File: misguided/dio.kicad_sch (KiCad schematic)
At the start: 0 parts

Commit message: buncha stuff
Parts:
- added CR401, CR402: LTV-217-TP1-C-G, LTV_217_LTO, symbol misguided:LTV-217-TP1-C-G
- added R401: 1k, symbol Device:R
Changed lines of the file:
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@@
 (kicad_sch (version 20230121) (generator eeschema)
   (paper "A4")
+  (hierarchical_label "DOUT_REF" (shape input) (at 131.445 92.71 0) (fields_autoplaced)
+    (effects (font (size 1.27 1.27)) (justify left))
+  )
+  (hierarchical_label "DOUT" (shape output) (at 121.92 95.25 0) (fields_autoplaced)
+    (effects (font (size 1.27 1.27)) (justify left))
+  )
+  (hierarchical_label "OUTPUT_GPIO" (shape input) (at 96.52 95.25 180) (fields_autoplaced)
+    (effects (font (size 1.27 1.27)) (justify right))
+  )
+  (hierarchical_label "DOUT_GND" (shape input) (at 132.08 100.33 0) (fields_autoplaced)
+    (effects (font (size 1.27 1.27)) (justify left))
+  )
+  (hierarchical_label "DIN" (shape input) (at 121.92 64.135 0) (fields_autoplaced)
+    (effects (font (size 1.27 1.27)) (justify left))
+  )
+  (hierarchical_label "DIN_GND" (shape input) (at 121.92 66.04 0) (fields_autoplaced)
+    (effects (font (size 1.27 1.27)) (justify left))
+  )
+  (hierarchical_label "INPUT_GPIO" (shape output) (at 96.52 64.135 180) (fields_autoplaced)
+    (effects (font (size 1.27 1.27)) (justify right))
+  )
+  (symbol (lib_id "Device:R") (at 119.38 90.17 0) (unit 1)
+    (in_bom yes) (on_board yes) (dnp no) (fields_autoplaced)
+    (property "Reference" "R401" (at 121.92 89.535 0)
+      (effects (font (size 1.27 1.27)) (justify left))
+    )
+    (property "Value" "1k" (at 121.92 92.075 0)
+      (effects (font (size 1.27 1.27)) (justify left))
+    )
+    (property "Footprint" "" (at 117.602 90.17 90)
+      (effects (font (size 1.27 1.27)) hide)
+    )
+    (property "Datasheet" "~" (at 119.38 90.17 0)
+      (effects (font (size 1.27 1.27)) hide)
+    )
+    (pin "1")
+    (pin "2")
+    (instances
+      (project "misguided"
+        (path "/2c6152e0-1c3c-4f15-8d1e-fd42bd51bc79/6cc4a32d-403e-4907-919c-d415739d9e80"
+          (reference "R401") (unit 1)
+        )
+      )
+    )
+  )
+  (symbol (lib_id "misguided:LTV-217-TP1-C-G") (at 103.505 111.76 0) (unit 1)
+    (in_bom yes) (on_board yes) (dnp no) (fields_autoplaced)
+    (property "Reference" "CR402" (at 103.505 104.14 0)
+      (effects (font (size 1.524 1.524)))
+    )
+    (property "Value" "LTV-217-TP1-C-G" (at 103.505 106.68 0)
+      (effects (font (size 1.524 1.524)))
+    )
+    (property "Footprint" "LTV_217_LTO" (at 103.505 119.38 0)
+      (effects (font (size 1.27 1.27) italic) hide)
+    )
+    (property "Datasheet" "LTV-217-TP1-C-G" (at 103.505 121.92 0)
+      (effects (font (size 1.27 1.27) italic) hide)
+    )
+    (pin "1")
+    (pin "2")
+    (pin "3")
+    (pin "4")
+    (instances
+      (project "misguided"
+        (path "/2c6152e0-1c3c-4f15-8d1e-fd42bd51bc79/6cc4a32d-403e-4907-919c-d415739d9e80"
+          (reference "CR402") (unit 1)
+        )
+      )
+    )
+  )
+  (symbol (lib_id "misguided:LTV-217-TP1-C-G") (at 105.41 74.93 0) (unit 1)
+    (in_bom yes) (on_board yes) (dnp no) (fields_autoplaced)
+    (property "Reference" "CR401" (at 105.41 67.31 0)
+      (effects (font (size 1.524 1.524)))
+    )
+    (property "Value" "LTV-217-TP1-C-G" (at 105.41 69.85 0)
+      (effects (font (size 1.524 1.524)))
+    )
+    (property "Footprint" "LTV_217_LTO" (at 105.41 82.55 0)
+      (effects (font (size 1.27 1.27) italic) hide)
+    )
+    (property "Datasheet" "LTV-217-TP1-C-G" (at 105.41 85.09 0)
+      (effects (font (size 1.27 1.27) italic) hide)
+    )
+    (pin "1")
+    (pin "2")
+    (pin "3")
+    (pin "4")
+    (instances
+      (project "misguided"
+        (path "/2c6152e0-1c3c-4f15-8d1e-fd42bd51bc79/6cc4a32d-403e-4907-919c-d415739d9e80"
+          (reference "CR401") (unit 1)
+        )
+      )
+    )
+  )
 )

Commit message: more setup
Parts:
- added R402, R403, R404: 1k, Resistor_SMD:R_0603_1608Metric, symbol Device:R
- CR?: renamed from CR402; footprint LTV_217_LTO -> misguided:LTV_217_LTO
- CR?: renamed from CR401; footprint LTV_217_LTO -> misguided:LTV_217_LTO
- R401: footprint (none) -> Resistor_SMD:R_0603_1608Metric
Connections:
- net DIN: now also R402.1
- net DIN_GND: now also CR?.2 (CATHODE)
- net DOUT: now also CR?.4 (COLLECTOR), R404.2
- net DOUT_GND: now also CR?.3 (EMITTER)
- net DOUT_REF: now also R404.1
- net INPUT_GPIO: now also CR?.4 (COLLECTOR), R401.2
- net OUTPUT_GPIO: now also R403.1
- net +3.3V: now reaches R401.1
- net at CR?.1 (ANODE): now also R403.2
- net GND: now reaches CR?.2 (CATHODE)
- net GND: now also CR?.3 (EMITTER)
- net at CR?.1 (ANODE): now also R402.2

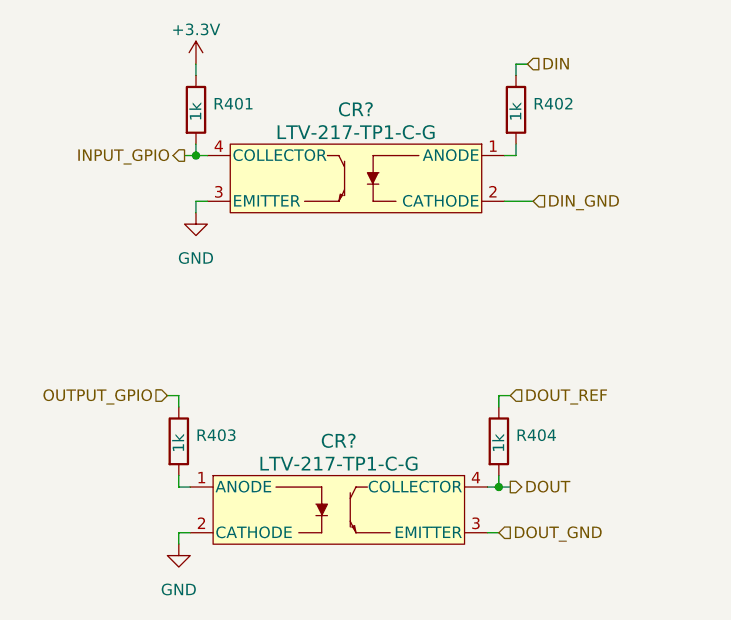
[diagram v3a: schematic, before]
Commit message: fixed schematic associations
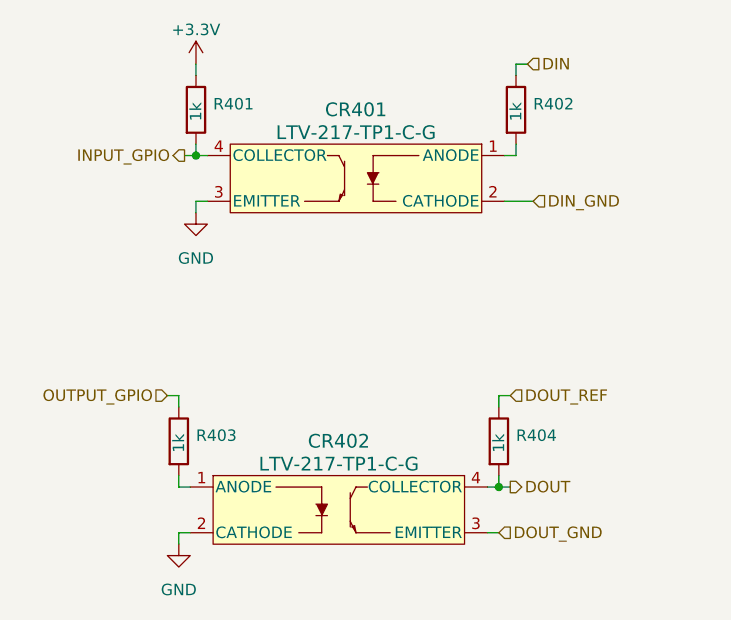
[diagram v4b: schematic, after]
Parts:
- gave numbers to parts that had none: 2
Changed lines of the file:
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@@
   (symbol (lib_id "power:+3.3V") (at 87.63 62.23 0) (unit 1)
     (in_bom yes) (on_board yes) (dnp no) (fields_autoplaced)
-    (property "Reference" "#PWR0403" (at 87.63 66.04 0)
+    (property "Reference" "#PWR0401" (at 87.63 66.04 0)
       (effects (font (size 1.27 1.27)) hide)
     )
@@
       (project "misguided"
         (path "/2c6152e0-1c3c-4f15-8d1e-fd42bd51bc79/6cc4a32d-403e-4907-919c-d415739d9e80"
-          (reference "#PWR0403") (unit 1)
+          (reference "#PWR0401") (unit 1)
         )
       )
@@
   (symbol (lib_id "power:GND") (at 85.725 115.57 0) (unit 1)
     (in_bom yes) (on_board yes) (dnp no) (fields_autoplaced)
-    (property "Reference" "#PWR0402" (at 85.725 121.92 0)
+    (property "Reference" "#PWR0403" (at 85.725 121.92 0)
       (effects (font (size 1.27 1.27)) hide)
     )
@@
       (project "misguided"
         (path "/2c6152e0-1c3c-4f15-8d1e-fd42bd51bc79/6cc4a32d-403e-4907-919c-d415739d9e80"
-          (reference "#PWR0402") (unit 1)
+          (reference "#PWR0403") (unit 1)
         )
       )
@@
   (symbol (lib_id "misguided:LTV-217-TP1-C-G") (at 103.505 111.76 0) (unit 1)
     (in_bom yes) (on_board yes) (dnp no) (fields_autoplaced)
-    (property "Reference" "CR?" (at 103.505 104.14 0)
+    (property "Reference" "CR402" (at 103.505 104.14 0)
       (effects (font (size 1.524 1.524)))
     )
@@
       (project "misguided"
         (path "/2c6152e0-1c3c-4f15-8d1e-fd42bd51bc79/6cc4a32d-403e-4907-919c-d415739d9e80"
-          (reference "CR?") (unit 1)
+          (reference "CR402") (unit 1)
         )
       )
@@
   (symbol (lib_id "power:GND") (at 87.63 78.74 0) (unit 1)
     (in_bom yes) (on_board yes) (dnp no) (fields_autoplaced)
-    (property "Reference" "#PWR0401" (at 87.63 85.09 0)
+    (property "Reference" "#PWR0402" (at 87.63 85.09 0)
       (effects (font (size 1.27 1.27)) hide)
     )
@@
       (project "misguided"
         (path "/2c6152e0-1c3c-4f15-8d1e-fd42bd51bc79/6cc4a32d-403e-4907-919c-d415739d9e80"
-          (reference "#PWR0401") (unit 1)
+          (reference "#PWR0402") (unit 1)
         )
       )
@@
   (symbol (lib_id "misguided:LTV-217-TP1-C-G") (at 105.41 74.93 0) (mirror y) (unit 1)
     (in_bom yes) (on_board yes) (dnp no)
-    (property "Reference" "CR?" (at 105.41 67.31 0)
+    (property "Reference" "CR401" (at 105.41 67.31 0)
       (effects (font (size 1.524 1.524)))
     )
@@
       (project "misguided"
         (path "/2c6152e0-1c3c-4f15-8d1e-fd42bd51bc79/6cc4a32d-403e-4907-919c-d415739d9e80"
-          (reference "CR?") (unit 1)
+          (reference "CR401") (unit 1)
         )
       )
